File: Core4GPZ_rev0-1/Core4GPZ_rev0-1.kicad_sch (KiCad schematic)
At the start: 3 parts, among them U2 core4, U3 MPXHZ6250AC6T1

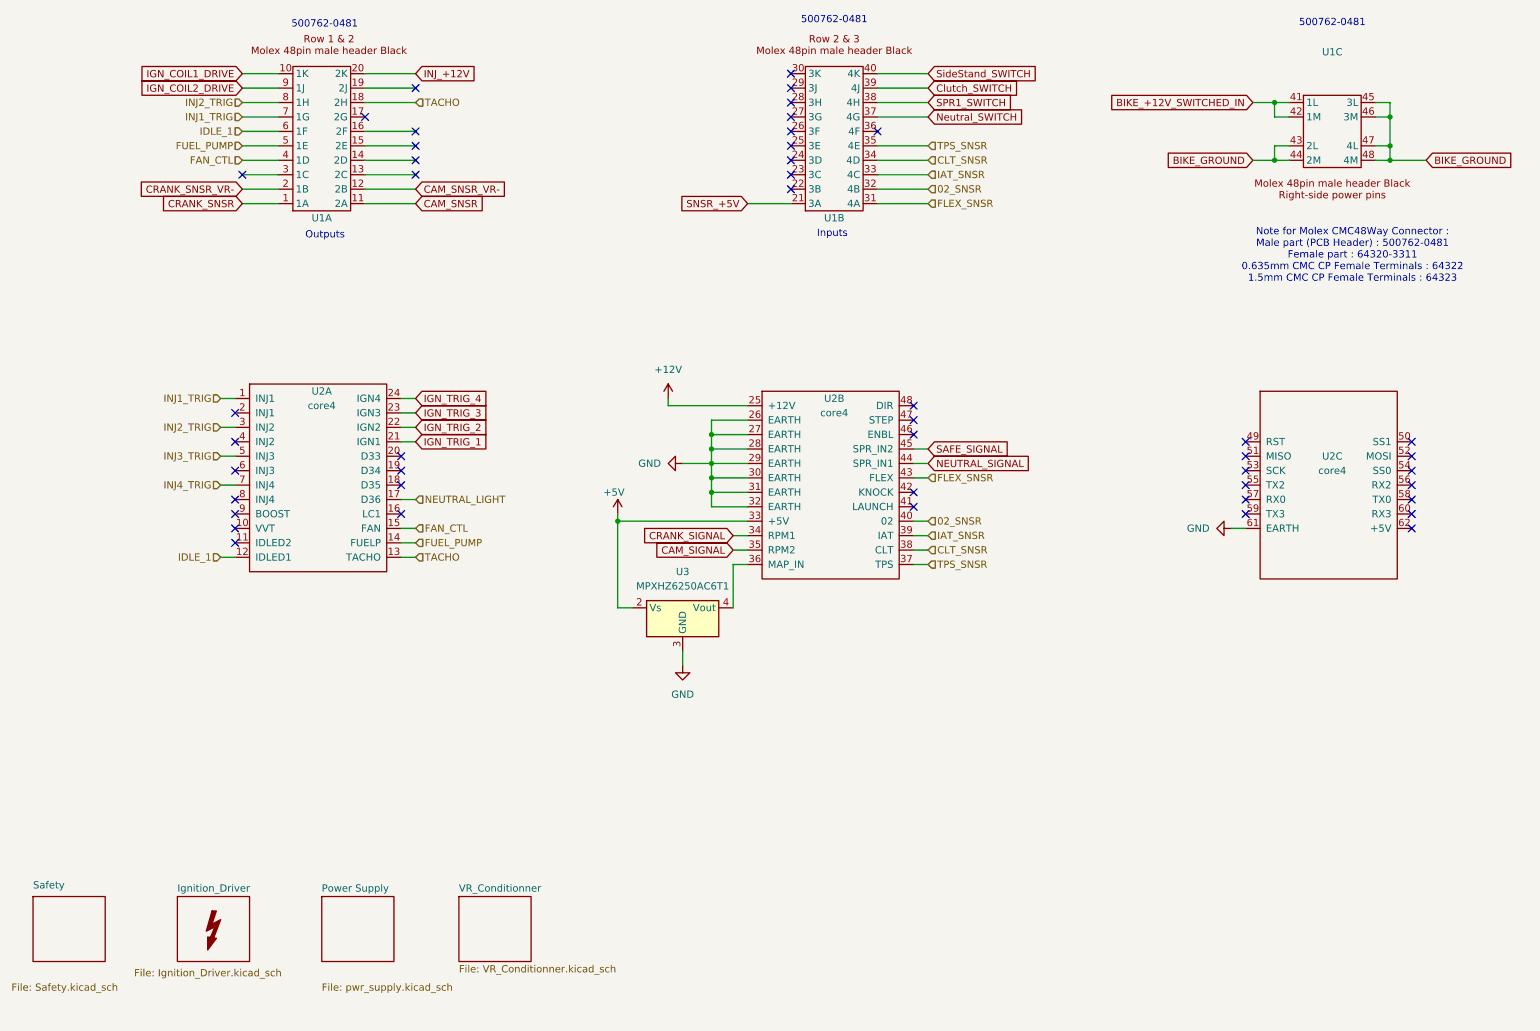
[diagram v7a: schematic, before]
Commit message: Started implementing Stepper driver
DRV8825 breakout board
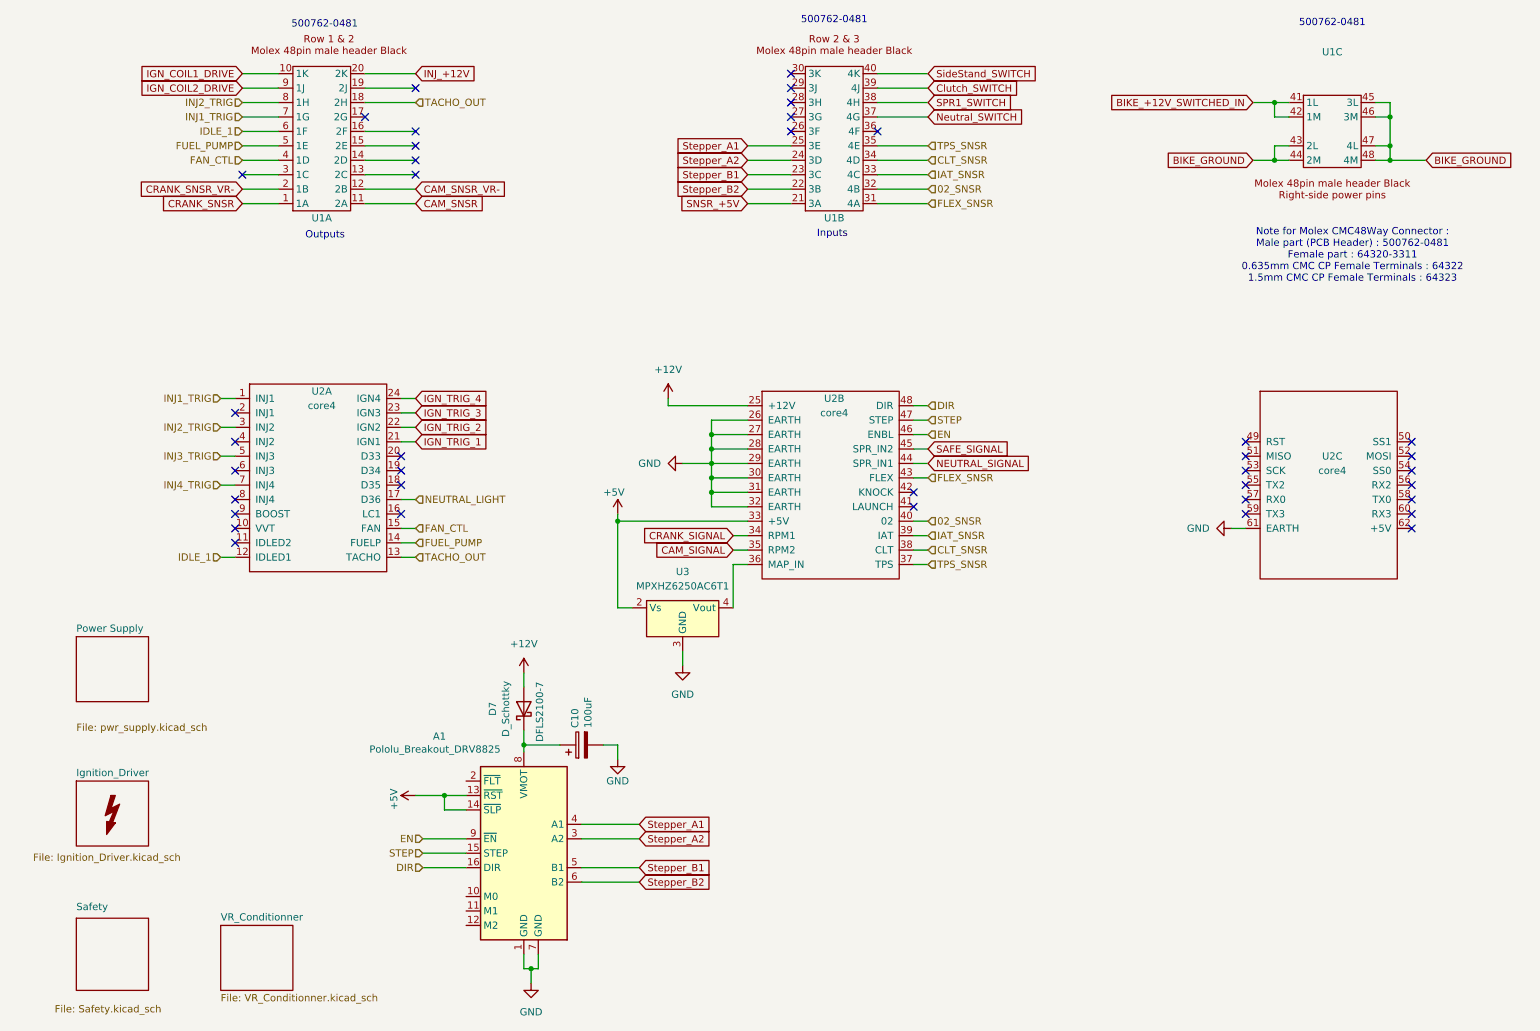
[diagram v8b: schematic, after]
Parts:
- added A1: Pololu_Breakout_DRV8825, Module:Pololu_Breakout-16_15.2x20.3mm, symbol Driver_Motor:Pololu_Breakout_DRV8825
- added C10: 100uF, Capacitor_SMD:CP_Elec_6.3x7.7, symbol Device:CP
- added D7: D_Schottky, Diode_SMD:D_PowerDI-123, symbol Device:D_Schottky
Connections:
- net +12V: now also D7.2 (A)
- net +5V: now also A1.13 (~{RST}), A1.14 (~{SLP})
- net GND: now also A1.1 (GND), A1.7 (GND), C10.2
- net EN: now reaches U2.46 (ENBL)
- net EN: now also A1.9 (~{EN})
- net STEP: now reaches U2.47 (STEP)
- net STEP: now also A1.15 (STEP)
- net DIR: now reaches U2.48 (DIR)
- net DIR: now also A1.16 (DIR)
- net Stepper_B2: now reaches U1.22 (3B)
- net Stepper_B2: now also A1.6 (B2)
- net Stepper_B1: now reaches U1.23 (3C)
- net Stepper_B1: now also A1.5 (B1)
- net Stepper_A2: now reaches U1.24 (3D)
- net Stepper_A2: now also A1.3 (A2)
- net Stepper_A1: now reaches U1.25 (3E)
- net Stepper_A1: now also A1.4 (A1)
- net TACHO renamed TACHO_OUT
- new net: A1.8 (VMOT), C10.1, D7.1 (K)
- no-connect marks 46 -> 39
